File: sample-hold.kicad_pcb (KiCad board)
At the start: 2 copper layers, 11 parts, among them J1 Conn_02x05_Odd_Even

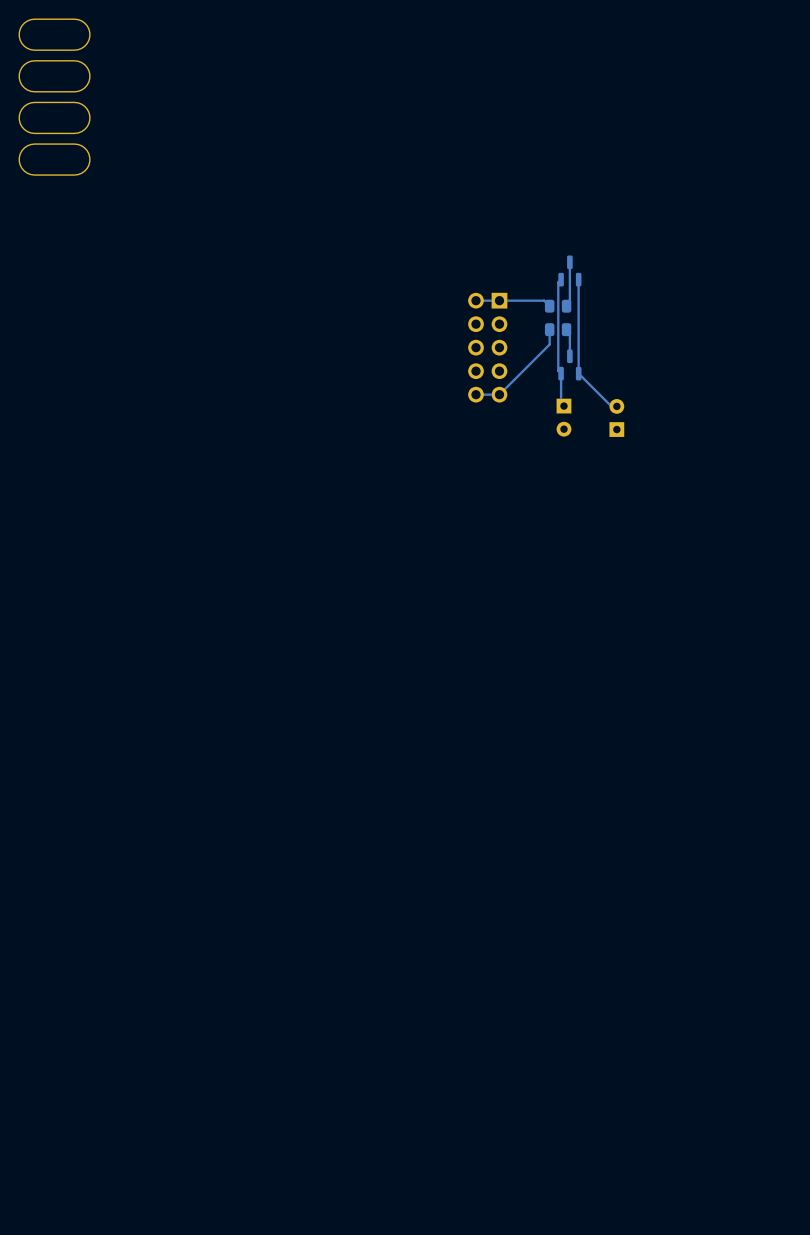
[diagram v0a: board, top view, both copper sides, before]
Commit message: adding rate knob and internal clock
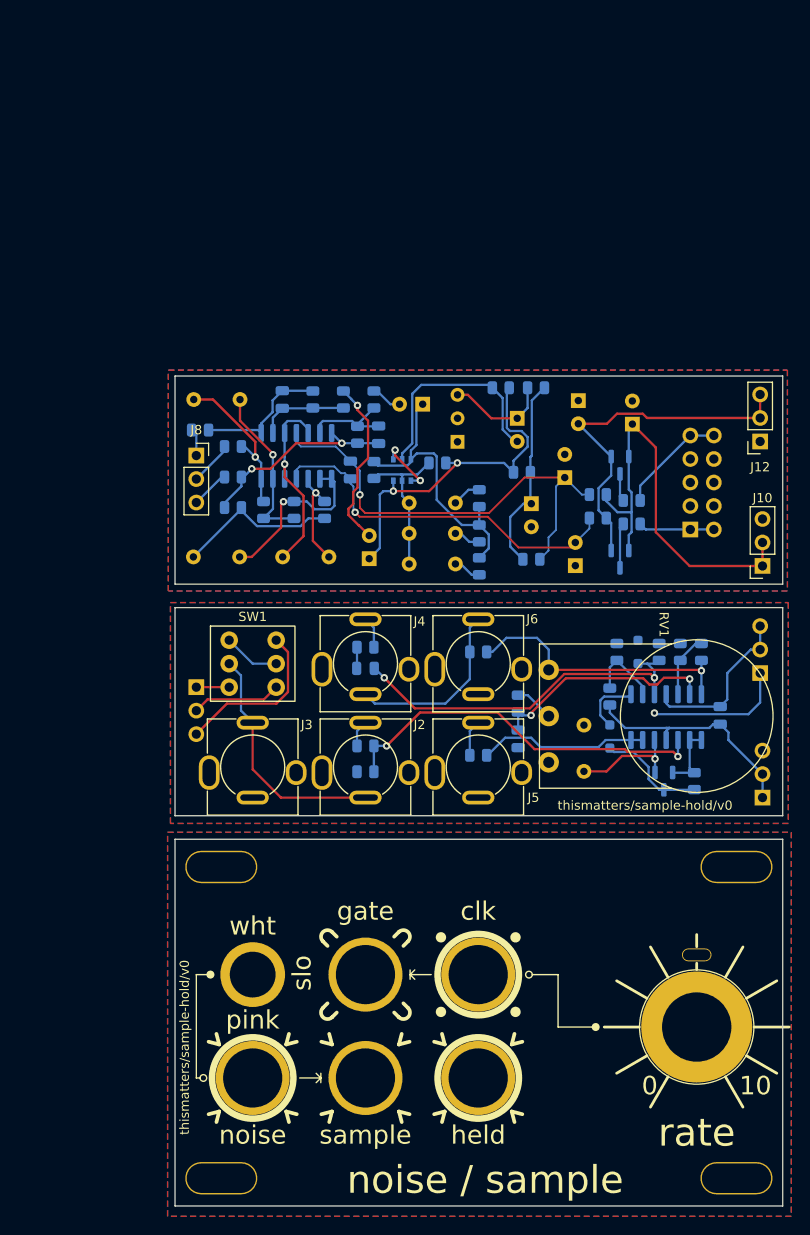
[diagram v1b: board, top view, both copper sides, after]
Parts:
- added C10: 47n box, Capacitor_THT:C_Rect_L7.2mm_W2.5mm_P5.00mm_FKS2_FKP2_MKS2_MKP2, B.Cu at (75.3, 67.6)
- added C11: 1n box, Capacitor_THT:C_Rect_L7.2mm_W2.5mm_P5.00mm_FKS2_FKP2_MKS2_MKP2, B.Cu at (75.3, 74.2)
- added C12: 3.3n box, Capacitor_THT:C_Rect_L7.2mm_W2.5mm_P5.00mm_FKS2_FKP2_MKS2_MKP2, B.Cu at (75.3, 70.9)
- added C13: 10u 35V, Capacitor_THT:CP_Radial_D5.0mm_P2.50mm, B.Cu at (76.8, 57.0)
- added C14: 10p, Capacitor_SMD:C_0805_2012Metric, B.Cu at (72.0, 60.3)
- added C15: 1u box, Capacitor_THT:C_Rect_L7.2mm_W5.5mm_P5.00mm_FKS2_FKP2_MKS2_MKP2, B.Cu at (52.0, 73.5)
- added C16: 1u box, Capacitor_THT:C_Rect_L7.2mm_W5.5mm_P5.00mm_FKS2_FKP2_MKS2_MKP2, B.Cu at (61.7, 73.5)
- added C17: 150n box, Capacitor_THT:C_Rect_L7.2mm_W3.5mm_P5.00mm_FKS2_FKP2_MKS2_MKP2, B.Cu at (57.0, 56.4)
- added C18: 100n, Capacitor_SMD:C_0805_2012Metric, B.Cu at (109.0, 90.6)
- added C19: 1n, Capacitor_SMD:C_0805_2012Metric, B.Cu at (70.6, 85.5)
- added C20: 100n box, Capacitor_THT:C_Rect_L7.2mm_W2.5mm_P5.00mm_FKS2_FKP2_MKS2_MKP2, B.Cu at (94.2, 96.6)
- added C21: 10u, Capacitor_SMD:C_0805_2012Metric, B.Cu at (87.1, 93.1)
- added C3: 22u 50V, Capacitor_THT:CP_Radial_D5.0mm_P2.50mm, B.Cu at (92.2, 64.9)
- added C4: 22u 50V, Capacitor_THT:CP_Radial_D5.0mm_P2.50mm, B.Cu at (93.3, 74.4)
- added C5: 47u 50V, Capacitor_THT:CP_Radial_D6.3mm_P2.50mm, B.Cu at (88.5, 67.7)
- added C6: 47u 50V, Capacitor_THT:CP_Radial_D6.3mm_P2.50mm, B.Cu at (87.0, 58.5)
- added C7: 100n, Capacitor_SMD:C_0805_2012Metric, B.Cu at (69.0, 64.1)
- added C8: 10u 35V, Capacitor_THT:CP_Radial_D5.0mm_P2.50mm, B.Cu at (71.0, 73.7)
- added C9: 10p, Capacitor_SMD:C_0805_2012Metric, B.Cu at (61.6, 56.4)
- added D3: 1N4148, Diode_SMD:D_SOD-323_HandSoldering, B.Cu at (100.1, 83.7)
- added D4: 1N4148, Diode_SMD:D_SOD-323_HandSoldering, B.Cu at (97.0, 92.9)
- added H10: clock, Eurorack:Mech-AudioJack-Hole-Output-Clock, F.Cu at (82.8, 118.6)
- added H11: rate, Eurorack:Mech-Potentiometer-Hole_level_90deg, F.Cu at (106.4, 124.3)
- added H5: gate, Eurorack:Mech-AudioJack-Hole-Input-Gate, F.Cu at (70.6, 118.6)
- added H6: in, Eurorack:Mech-AudioJack-Hole-Input-Voct, F.Cu at (70.6, 129.8)
- added H7: rand, Eurorack:Mech-AudioJack-Hole-Output-Voct, F.Cu at (58.4, 129.8)
- added H8: out, Eurorack:Mech-AudioJack-Hole-Output-Voct, F.Cu at (82.8, 129.8)
- added H9: switch, Eurorack:Mech-2M_Switch-Hole, F.Cu at (58.4, 118.6)
- added J10: Conn_01x03_Socket, Connector_PinSocket_2.54mm:PinSocket_1x03_P2.54mm_Vertical, F.Cu at (113.5, 74.4)
- added J11: Conn_01x03_Pin, Connector_PinHeader_2.54mm:PinHeader_1x03_P2.54mm_Vertical, B.Cu at (113.3, 86.0)
- added J12: Conn_01x03_Socket, Connector_PinSocket_2.54mm:PinSocket_1x03_P2.54mm_Vertical, F.Cu at (113.3, 61.0)
- added J2: AudioJack2_SwitchT, Eurorack:AudioJack2_Tayda_A-2566, F.Cu at (70.6, 96.2)
- added J3: AudioJack2_SwitchT, Eurorack:AudioJack2_Tayda_A-2566, F.Cu at (58.4, 96.2)
- added J4: AudioJack2_SwitchT, Eurorack:AudioJack2_Tayda_A-2566, F.Cu at (70.6, 85.0)
- added J5: AudioJack2_SwitchT, Eurorack:AudioJack2_Tayda_A-2566, F.Cu at (82.8, 96.2)
- added J6: AudioJack2_SwitchT, Eurorack:AudioJack2_Tayda_A-2566, F.Cu at (82.8, 85.0)
- added J7: Conn_01x03_Pin, Connector_PinHeader_2.54mm:PinHeader_1x03_P2.54mm_Vertical, B.Cu at (52.3, 87.5)
- added J8: Conn_01x03_Socket, Connector_PinSocket_2.54mm:PinSocket_1x03_P2.54mm_Vertical, F.Cu at (52.3, 62.5)
- added J9: Conn_01x03_Pin, Connector_PinHeader_2.54mm:PinHeader_1x03_P2.54mm_Vertical, B.Cu at (113.5, 99.5)
- added Q1: BC547C, Package_TO_SOT_THT:TO-92_Inline_Wide, B.Cu at (80.6, 61.0)
- added Q2: BCM847, Package_SO:TSOP-6_1.65x3.05mm_P0.95mm, B.Cu at (74.6, 64.1)
- added Q3: MMBF4393, Package_TO_SOT_SMD:SOT-23, B.Cu at (102.9, 97.7)
- added R10: 470K, Resistor_SMD:R_0805_2012Metric, B.Cu at (64.9, 56.4)
- added R11: 1K, Resistor_SMD:R_0805_2012Metric, B.Cu at (52.7, 59.7)
- added R12: 82K, Resistor_SMD:R_0805_2012Metric, B.Cu at (78.4, 63.3)
- added R13: 100K, Resistor_SMD:R_0805_2012Metric, B.Cu at (82.9, 70.9)
- added R14: 18K, Resistor_SMD:R_0805_2012Metric, B.Cu at (82.9, 74.5)
- added R15: 390K, Resistor_SMD:R_0805_2012Metric, B.Cu at (82.9, 67.1)
- added R16: 1M, Resistor_SMD:R_0805_2012Metric, B.Cu at (71.5, 64.1)
- added R17: 8.2K, Resistor_SMD:R_0805_2012Metric, B.Cu at (71.5, 56.4)
- added R18: 470K, Resistor_SMD:R_0805_2012Metric, B.Cu at (69.7, 60.3)
- added R19: 1K, Resistor_SMD:R_0805_2012Metric, B.Cu at (56.3, 64.8)
- added R20: 33K, Resistor_SMD:R_0805_2012Metric, B.Cu at (56.3, 68.1)
- added R21: 33K, Resistor_SMD:R_0805_2012Metric, B.Cu at (66.2, 68.4)
- added R22: 10K, Resistor_SMD:R_0805_2012Metric, B.Cu at (62.9, 68.4)
- added R23: 220K, Resistor_SMD:R_0805_2012Metric, B.Cu at (59.6, 68.4)
- added R24: 1K, Resistor_SMD:R_0805_2012Metric, B.Cu at (56.3, 61.5)
- added R25: 1K, Resistor_SMD:R_0805_2012Metric, B.Cu at (70.6, 83.2)
- added R26: 100K, Resistor_SMD:R_0805_2012Metric, B.Cu at (102.4, 83.7)
- added R27: 100K, Resistor_SMD:R_0805_2012Metric, B.Cu at (97.0, 88.6)
- added R28: 10K, Resistor_SMD:R_0805_2012Metric, B.Cu at (97.8, 83.7)
- added R29: 100K, Resistor_SMD:R_0805_2012Metric, B.Cu at (70.6, 96.7)
- added R3: 10, Resistor_SMD:R_0805_2012Metric, B.Cu at (95.7, 69.3)
- added R30: 100, Resistor_SMD:R_0805_2012Metric, B.Cu at (70.6, 93.9)
- added R31: 2.2M, Resistor_SMD:R_0805_2012Metric, B.Cu at (106.2, 97.7)
- added R32: 1K, Resistor_SMD:R_0805_2012Metric, B.Cu at (82.8, 94.9)
- added R33: 2.2K, Resistor_SMD:R_0805_2012Metric, B.Cu at (87.1, 89.3)
- added R34: 100K, Resistor_SMD:R_0805_2012Metric, B.Cu at (104.6, 83.7)
- added R35: 120K, Resistor_SMD:R_0805_2012Metric, B.Cu at (106.9, 83.7)
- added R36: 1K, Resistor_SMD:R_0805_2012Metric, B.Cu at (82.8, 83.7)
- added R4: 10, Resistor_SMD:R_0805_2012Metric, B.Cu at (95.7, 66.7)
- added R5: 47K, Resistor_SMD:R_0805_2012Metric, B.Cu at (89.1, 55.2)
- added R6: 150K, Resistor_SMD:R_0805_2012Metric, B.Cu at (85.2, 55.2)
- added R7: 10K, Resistor_SMD:R_0805_2012Metric, B.Cu at (87.5, 64.3)
- added R8: 22, Resistor_SMD:R_0805_2012Metric, B.Cu at (88.5, 73.7)
- added R9: 33K, Resistor_SMD:R_0805_2012Metric, B.Cu at (68.2, 56.4)
- added RV1: C500K, Eurorack:Potentiometer_RV16AF-41-15R1, F.Cu at (106.4, 90.7)
- added SW1: ON-ON-ON, Eurorack:Switch_DPDT_Tayda_A-5752, F.Cu at (58.4, 85.0)
- added U1: TL074, Package_SO:SOIC-14_3.9x8.7mm_P1.27mm, B.Cu at (63.1, 62.5)
- added U2: TL074, Package_SO:SOIC-14_3.9x8.7mm_P1.27mm, B.Cu at (103.1, 90.8)
- moved H3 136.3 mm to (110.7, 140.6)
- moved H2 112.9 mm to (110.7, 107.0)
- moved H4 111.6 mm to (55.0, 140.6)
- moved H1 91.8 mm to (55.0, 107.0)
- moved J1 32.2 mm to (105.7, 70.5), turned to 0 degrees
- moved D1 31.6 mm to (98.1, 73.7), turned to -90 degrees
- moved R2 24.9 mm to (99.4, 69.9), turned to 0 degrees
- moved R1 20.1 mm to (99.4, 67.4), turned to 0 degrees
- moved D2 12.1 mm to (98.1, 63.5), turned to -90 degrees
- moved C1 7.65 mm to (99.5, 59.1), turned to 90 degrees
- moved C2 5.21 mm to (93.6, 56.6), turned to -90 degrees
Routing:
- net /+12: track 0.00 -> 50.5 mm, vias 0 -> 1
- net Net-(U2A-+): track 0.00 -> 40.9 mm, vias 0 -> 2
- net /-12: track 0.00 -> 40.2 mm, vias 0 -> 1
- net Net-(D3-K): track 0.00 -> 39.2 mm, vias 0 -> 2
- net Net-(Q2A-C1): track 0.00 -> 37.2 mm, vias 0 -> 2
- net +12V: track 14.0 -> 45.9 mm
- net Net-(R35-Pad2): track 0.00 -> 30.3 mm, vias 0 -> 1
- net Net-(Q2B-C2): track 0.00 -> 30.2 mm
- net GND: track 0.00 -> 27.3 mm, vias 0 -> 3
- net /RAND: track 0.00 -> 25.9 mm
- net /+12V': track 0.00 -> 25.3 mm
- net Net-(U2D--): track 0.00 -> 24.2 mm, vias 0 -> 2
- net -12V: track 15.8 -> 39.1 mm
- net Net-(Q2A-B1): track 0.00 -> 23.1 mm
- net Net-(C14-Pad2): track 0.00 -> 21.2 mm, vias 0 -> 2
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- added copper zone on B.Cu, net /FACE
- added copper zone on F.Cu, net /FACE
- added copper zone on B.Cu, net /GND'
- added copper zone on F.Cu, net /GND'
- added copper zone on B.Cu, net GND
- added copper zone on F.Cu, net GND
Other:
- board outline added: 65.7 x 89.7 mm
- board text added: "clk"
- board text added: "gate"
- board text added: "held"
- board text added: "noise"
- board text added: "noise / sample"
- board text added: "pink"
- board text added: "sample"
- board text added: "slo"
- board text added: "thismatters/sample-hold/v0"
- board text added: "wht"
- board text removed: "POWER"

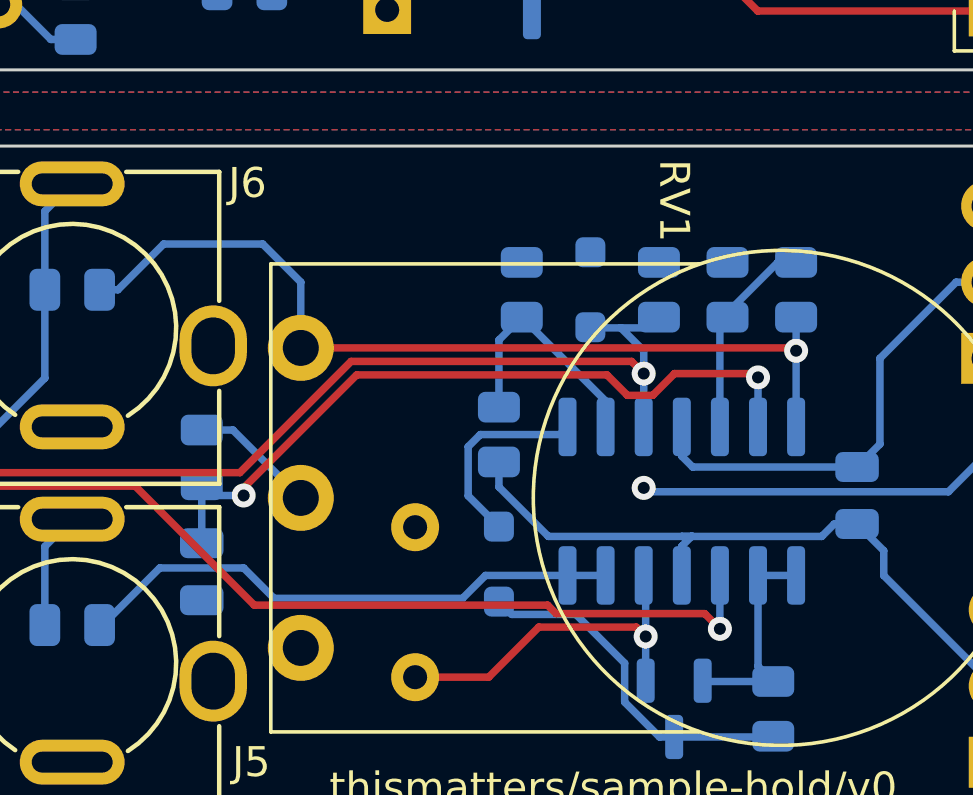
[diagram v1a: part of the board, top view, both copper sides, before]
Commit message: correct capacitor type
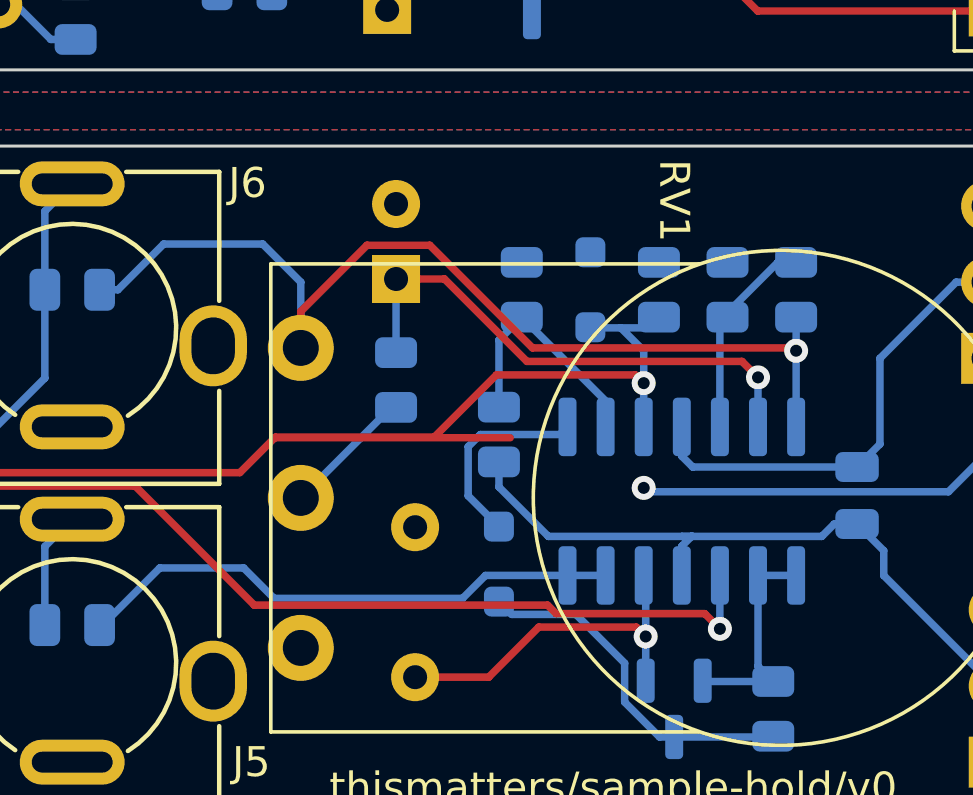
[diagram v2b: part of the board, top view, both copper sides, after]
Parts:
- C21: value 10u -> 10u 35V; footprint Capacitor_SMD:C_0805_2012Metric -> Capacitor_THT:CP_Radial_D5.0mm_P2.50mm
- moved C21 11.7 mm to (93.6, 83.4), turned to 90 degrees
- moved R33 6.97 mm to (93.6, 86.7), turned to -90 degrees
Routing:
- net Net-(D3-K): track 39.2 -> 46.9 mm
- net Net-(U2D--): track 24.2 -> 17.5 mm, vias 2 -> 1
- net Net-(R35-Pad2): track 30.3 -> 33.8 mm

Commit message: little routing cleanup
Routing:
- net Net-(D3-K): track 46.9 -> 39.0 mm
- net Net-(R35-Pad2): track 33.8 -> 30.6 mm
- net Net-(U2D--): track 17.5 -> 18.2 mm
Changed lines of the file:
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@@
   (segment (start 101.5795 86.571) (end 101.854 86.8455) (width 0.25) (layer "F.Cu") (net 30))
   (segment (start 89.555 88.666) (end 89.575 88.646) (width 0.25) (layer "F.Cu") (net 30))
-  (segment (start 89.555 88.666) (end 97.404 88.666) (width 0.25) (layer "F.Cu") (net 30))
   (segment (start 72.644 86.527) (end 75.946 89.829) (width 0.25) (layer "F.Cu") (net 30))
   (via (at 101.854 86.8455) (size 0.8) (drill 0.4) (layers "F.Cu" "B.Cu") (net 30))
@@
   (segment (start 85.723 93.006) (end 83.82 94.909) (width 0.25) (layer "B.Cu") (net 46))
   (segment (start 96.5799 93.255) (end 95.8149 94.02) (width 0.25) (layer "B.Cu") (net 46))
-  (segment (start 98.933 94.528) (end 103.886 94.528) (width 0.25) (layer "F.Cu") (net 47))
-  (segment (start 76.512 90.279) (end 84.905 90.279) (width 0.25) (layer "F.Cu") (net 47))
-  (segment (start 98.651 94.246) (end 98.933 94.528) (width 0.25) (layer "F.Cu") (net 47))
-  (segment (start 88.872 94.246) (end 98.651 94.246) (width 0.25) (layer "F.Cu") (net 47))
-  (segment (start 103.886 94.528) (end 104.394 95.036) (width 0.25) (layer "F.Cu") (net 47))
-  (segment (start 84.905 90.279) (end 88.872 94.246) (width 0.25) (layer "F.Cu") (net 47))
-  (segment (start 72.898 93.893) (end 76.512 90.279) (width 0.25) (layer "F.Cu") (net 47))
+  (segment (start 76.512 90.279) (end 72.898 93.893) (width 0.25) (layer "F.Cu") (net 47))
+  (segment (start 91.468 94.528) (end 91.186 94.246) (width 0.25) (layer "F.Cu") (net 47))
+  (segment (start 84.905 90.279) (end 76.512 90.279) (width 0.25) (layer "F.Cu") (net 47))
+  (segment (start 88.872 94.246) (end 84.905 90.279) (width 0.25) (layer "F.Cu") (net 47))
+  (segment (start 104.394 95.036) (end 103.886 94.528) (width 0.25) (layer "F.Cu") (net 47))
+  (segment (start 103.886 94.528) (end 91.468 94.528) (width 0.25) (layer "F.Cu") (net 47))
+  (segment (start 91.186 94.246) (end 88.872 94.246) (width 0.25) (layer "F.Cu") (net 47))
   (via (at 72.898 93.893) (size 0.8) (drill 0.4) (layers "F.Cu" "B.Cu") (net 47))
   (via (at 104.394 95.036) (size 0.8) (drill 0.4) (layers "F.Cu" "B.Cu") (net 47))
@@
   (segment (start 58.42 85.003) (end 60.96 85.003) (width 0.25) (layer "B.Cu") (net 49))
   (segment (start 55.88 82.463) (end 58.42 85.003) (width 0.25) (layer "B.Cu") (net 49))
-  (segment (start 95.212604 83.374113) (end 97.959491 86.121) (width 0.25) (layer "F.Cu") (net 50))
-  (segment (start 97.959491 86.121) (end 105.131 86.121) (width 0.25) (layer "F.Cu") (net 50))
-  (segment (start 93.599 83.374113) (end 95.212604 83.374113) (width 0.25) (layer "F.Cu") (net 50))
-  (segment (start 105.131 86.121) (end 105.664 86.654) (width 0.25) (layer "F.Cu") (net 50))
-  (via (at 105.664 86.654) (size 0.8) (drill 0.4) (layers "F.Cu" "B.Cu") (net 50))
-  (segment (start 105.664 86.654) (end 105.664 88.305) (width 0.25) (layer "B.Cu") (net 50))
+  (segment (start 102.340701 85.6705) (end 102.834201 86.164) (width 0.25) (layer "F.Cu") (net 50))
+  (segment (start 93.599 83.374113) (end 95.895888 85.671) (width 0.25) (layer "F.Cu") (net 50))
+  (segment (start 101.854 85.671) (end 101.8545 85.6705) (width 0.25) (layer "F.Cu") (net 50))
+  (segment (start 102.834201 86.164) (end 105.3895 86.164) (width 0.25) (layer "F.Cu") (net 50))
+  (segment (start 101.8545 85.6705) (end 102.340701 85.6705) (width 0.25) (layer "F.Cu") (net 50))
+  (segment (start 105.3895 86.164) (end 105.664 85.8895) (width 0.25) (layer "F.Cu") (net 50))
+  (segment (start 95.895888 85.671) (end 101.854 85.671) (width 0.25) (layer "F.Cu") (net 50))
+  (via (at 105.664 85.8895) (size 0.8) (drill 0.4) (layers "F.Cu" "B.Cu") (net 50))
   (segment (start 93.599 83.374113) (end 93.599 85.8285) (width 0.25) (layer "B.Cu") (net 50))
+  (segment (start 105.664 85.8895) (end 105.664 88.305) (width 0.25) (layer "B.Cu") (net 50))
   (segment (start 90.424 90.671) (end 93.4415 87.6535) (width 0.25) (layer "B.Cu") (net 52))
-  (segment (start 93.4415 87.6535) (end 93.599 87.6535) (width 0.25) (layer "B.Cu") (net 52))
   (segment (start 104.394 88.305) (end 104.394 84.8995) (width 0.25) (layer "B.Cu") (net 53))
   (segment (start 106.3225 82.8205) (end 106.934 82.8205) (width 0.25) (layer "B.Cu") (net 53))
   (segment (start 104.648 84.495) (end 106.3225 82.8205) (width 0.25) (layer "B.Cu") (net 53))
-  (segment (start 92.629887 82.249113) (end 94.724 82.249113) (width 0.25) (layer "F.Cu") (net 55))
-  (segment (start 106.807 85.765) (end 106.934 85.765) (width 0.25) (layer "F.Cu") (net 55))
-  (segment (start 90.424 84.455) (end 92.629887 82.249113) (width 0.25) (layer "F.Cu") (net 55))
-  (segment (start 106.713 85.671) (end 106.807 85.765) (width 0.25) (layer "F.Cu") (net 55))
-  (segment (start 98.145887 85.671) (end 106.713 85.671) (width 0.25) (layer "F.Cu") (net 55))
-  (segment (start 94.724 82.249113) (end 98.145887 85.671) (width 0.25) (layer "F.Cu") (net 55))
-  (segment (start 90.424 85.671) (end 90.424 84.455) (width 0.25) (layer "F.Cu") (net 55))
-  (via (at 106.934 85.765) (size 0.8) (drill 0.4) (layers "F.Cu" "B.Cu") (net 55))
+  (segment (start 102.154305 86.1205) (end 90.8735 86.1205) (width 0.25) (layer "F.Cu") (net 55))
+  (segment (start 90.8735 86.1205) (end 90.424 85.671) (width 0.25) (layer "F.Cu") (net 55))
+  (segment (start 106.934 86.614) (end 102.647805 86.614) (width 0.25) (layer "F.Cu") (net 55))
+  (segment (start 102.647805 86.614) (end 102.154305 86.1205) (width 0.25) (layer "F.Cu") (net 55))
+  (via (at 106.934 86.614) (size 0.8) (drill 0.4) (layers "F.Cu" "B.Cu") (net 55))
+  (segment (start 106.934 84.6455) (end 106.934 86.614) (width 0.25) (layer "B.Cu") (net 55))
   (segment (start 83.7165 83.733) (end 84.328 83.733) (width 0.25) (layer "B.Cu") (net 55))
-  (segment (start 106.934 84.6455) (end 106.934 85.765) (width 0.25) (layer "B.Cu") (net 55))
-  (segment (start 106.934 85.765) (end 106.934 88.305) (width 0.25) (layer "B.Cu") (net 55))
+  (segment (start 106.934 86.614) (end 106.934 88.305) (width 0.25) (layer "B.Cu") (net 55))
   (segment (start 84.328 83.733) (end 85.852 82.209) (width 0.25) (layer "B.Cu") (net 55))
   (segment (start 85.852 82.209) (end 89.154 82.209) (width 0.25) (layer "B.Cu") (net 55))

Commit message: prototype tested and updates made ready for v0 manu
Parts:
- added D5: 1N4148, Diode_SMD:D_SOD-323_HandSoldering, B.Cu at (87.2, 92.6)
- added R37: 100K, Resistor_SMD:R_0805_2012Metric, B.Cu at (76.6, 91.3)
- added R38: 100K, Resistor_SMD:R_0805_2012Metric, B.Cu at (103.1, 97.7)
- added R39: 100K, Resistor_SMD:R_0805_2012Metric, B.Cu at (106.3, 96.5)
- added R40: 100K, Resistor_SMD:R_0805_2012Metric, B.Cu at (106.3, 98.7)
- added R41: 3.9K, Resistor_SMD:R_0805_2012Metric, B.Cu at (76.2, 60.7)
- added R42: 24K, Resistor_SMD:R_0805_2012Metric, B.Cu at (109.9, 94.5)
- added R43: 33K, Resistor_SMD:R_0805_2012Metric, B.Cu at (109.9, 96.6)
- Q3: value MMBF4393 -> MMBFJ111
- R30: value 100 -> 100K
- moved R31 5.21 mm to (101.0, 97.7)
- moved Q3 4.70 mm to (98.2, 97.7)
- moved R12 1.60 mm to (78.3, 64.9)
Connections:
- C21 pad 2: /GND' -> /-12V'
- R29 pad 1: Net-(U2A-+) -> Net-(R29-Pad1)
- R30 pad 2: Net-(U2A-+) -> Net-(R29-Pad1)
- R35 pad 2: Net-(R35-Pad2) -> Net-(D5-A)
- R36 pad 1: Net-(R35-Pad2) -> Net-(D5-K)
- RV1 pad 1: Net-(R35-Pad2) -> unconnected-(RV1-Pad1)
- RV1 pad 3: unconnected-(RV1-Pad3) -> Net-(D5-A)
- U2 pad 14: Net-(R35-Pad2) -> Net-(D5-A)
- U2 pad 2: Net-(Q3-S) -> Net-(U2A--)
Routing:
- net Net-(R35-Pad2): track 30.6 -> 0.00 mm, vias 1 -> 0
- net Net-(D5-A): track 0.00 -> 30.3 mm, vias 0 -> 1
- net /-12V': track 18.1 -> 38.6 mm
- net Net-(R38-Pad2): track 0.00 -> 10.6 mm
- net Net-(D5-K): track 0.00 -> 8.91 mm
- net Net-(R29-Pad1): track 0.00 -> 8.01 mm
- net Net-(Q3-S): track 7.34 -> 15.0 mm
- net /+12: track 50.5 -> 57.8 mm
- net Net-(U2A--): track 0.00 -> 5.12 mm
- net GND: track 27.3 -> 22.4 mm, vias 3 -> 2
- net Net-(U2A-+): track 40.9 -> 36.6 mm
- net Net-(D4-A): track 11.7 -> 9.74 mm
- net Net-(Q2B-C2): track 30.2 -> 28.8 mm
- net Net-(Q2A-C1): track 37.2 -> 36.1 mm
- net /+12V': track 25.3 -> 26.3 mm
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
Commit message: sent out for manu
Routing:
- net /RAND: track 25.9 -> 23.4 mm
- net Net-(D4-A): track 9.74 -> 8.40 mm
- net Net-(U2A-+): track 36.6 -> 35.9 mm, vias 2 -> 0
- net Net-(D5-A): track 30.3 -> 29.7 mm
- net Net-(Q3-D): track 11.0 -> 11.6 mm
